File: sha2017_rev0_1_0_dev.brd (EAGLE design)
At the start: 95 x 86 mm, 116 parts, among them IC1 AP7215, IC2 CPT112, IC3 CP210X_USB_UART, IC4 ESP32WROOM32, IC5 MCP73833, IC6 FXL6408, M1 MOTOR10MM, Q1 MMBT2222A, Q2 MMBT2222A, Q3 SI1304 BDL, Q4 MOSFET-PCHANNEL, Q5 MMBT2222A, Q6 MOSFET-PCHANNEL, Q7 MMBT2222A, Q8 MMBT2222A, T1 SI2301DS, X1_ JST-PH3, X701 2908-05WB-MG

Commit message: placed most of the parts
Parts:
- removed GND, SIG, VDD: (no value), wirepad:SMD1,27-2,54
- removed JP1: M05X2SHD_SMD, SparkFun-Connectors:2X5-SHROUDED_SMD
- removed M1: MOTOR10MM, SparkFun-Electromechanical:VIBE-MOTOR-10MM
- added J2: (no value), EAGLE-BOARD-TO-BOARD_CONNECTORS-rev16c:610X12243021
- added R27, R28: 470R, rcl:R0603
- added U$1: MOTOR10MM, badge:VIBE-MOTOR-10MM
- moved C38 207.0 mm to (38.2, 50.1)
- moved R26 205.6 mm to (38.8, 43.8)
- moved IC6 202.0 mm to (38.7, 47.5)
- moved Q8 181.5 mm to (27.5, 54.5)
- moved R11 178.2 mm to (27.5, 52.0), turned to 180 degrees
- moved R25 175.0 mm to (23.2, 52.0)
- moved C37 173.1 mm to (20.7, 53.7), turned to 270 degrees
- moved Q6 172.4 mm to (23.2, 54.6)
- moved R12 172.3 mm to (75.6, 78.6), turned to 180 degrees
- moved Q7 170.7 mm to (71.6, 76.7)
- moved R13 169.4 mm to (70.6, 73.1), turned to 270 degrees
- moved FD2 166.6 mm to (94.6, 86.4)
- moved D14 160.4 mm to (59.9, 74.0)
- moved R16 160.4 mm to (57.1, 74.9)
- moved T1 160.4 mm to (59.9, 76.8)
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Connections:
- removed net N$44: M1.+, R12.1
- removed net WS2812_POWER1: R11.1
- new net N$16: Q7.3, U$1.-
- new net WS2812_DATA_OUT: D9.2, J2.5
- new net WS2812_POWER_EN: IC6.12, R11.1, R18.1
- net +3V3: now also R27.1, R28.1
- net 3V3_SWITCHED: now also J2.12; no longer JP1.1
- net EXTIO-0: now also IC4.9, J2.10; no longer IC4.7, JP1.3
- net EXTIO-1: now also J2.9; no longer JP1.5
- net EXTIO-2: now also J2.8; no longer JP1.7
- net EXTIO-3: now also J2.4; no longer JP1.8
- net EXTIO-4: now also J2.3; no longer JP1.6
- net EXTIO-5: now also J2.2; no longer JP1.4
- net GND: now also J2.1; no longer GND.1, JP1.2, JP1.9
- net I2C_SCL: now also J2.6, R27.2
- net I2C_SDA: now also J2.7, R28.2
- net N$18: now also R12.1, U$1.+; no longer M1.-, Q7.3
- net VBAT: no longer R12.2
- net VBAT_SENSE: now also IC4.7; no longer IC4.9
- net VCC: now also R12.2
- net VUSB_SENSE: now also IC4.6; no longer IC4.8
- net WS2812_DATA: now also IC4.8; no longer IC4.6, SIG.1
- net WS2812_POWER: now also J2.11; no longer IC6.12, JP1.10, R18.1, VDD.1
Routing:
- net LCD_MOSI: track 25.6 -> 13.4 mm
- net LCD_SCK: track 23.6 -> 12.4 mm
- net LCD_CS: track 21.3 -> 11.2 mm
- net VCC: track 13.9 -> 4.67 mm, vias 1 -> 0
- net LCD_D/!S: track 19.0 -> 10.2 mm
- net LCD_!RESET: track 16.8 -> 8.65 mm
- net +3V3: track 11.9 -> 6.54 mm
- net PROXIMITY: track 228.7 -> 224.8 mm
- net +5V: track 34.3 -> 32.9 mm
- net VUSB_SENSE: track 5.10 -> 5.60 mm
- net GND: track 17.5 -> 17.6 mm, vias 63 -> 55
- removed copper zone on layer 16, net VCC
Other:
- board text removed: "MarkusBec"
- board text removed: "RESET"
- board text removed: "SHA Rev0.0.1 Dev"

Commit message: finised routing
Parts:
- removed J2: (no value), EAGLE-BOARD-TO-BOARD_CONNECTORS-rev16c:610X12243021
- added J3: (no value), EAGLE-BOARD-TO-BOARD_CONNECTORS-rev16c:610X12243021
- added S1, S2: SWITCH-MOMENTARY-2SMD, SparkFun-Electromechanical:TACTILE-SWITCH-SMD
- moved R28 76.4 mm to (20.4, 56.5), turned to 90 degrees
- moved R27 73.2 mm to (22.0, 56.5), turned to 90 degrees
- moved R8 29.9 mm to (15.4, 56.5)
- moved C36 22.5 mm to (39.0, 75.3), turned to 180 degrees
- moved R22 20.7 mm to (39.0, 73.8), turned to 0 degrees
- moved R17 16.8 mm to (53.2, 60.7)
- moved R20 16.8 mm to (53.2, 62.4)
- moved C34 16.6 mm to (53.2, 63.9)
- moved R21 15.8 mm to (42.3, 73.8), turned to 0 degrees
- moved C38 11.8 mm to (47.9, 43.3), turned to 270 degrees
- moved IC6 11.7 mm to (50.3, 46.2), turned to 270 degrees
- moved R26 10.6 mm to (49.4, 43.3), turned to 90 degrees
- moved C37 7.81 mm to (22.0, 46.0), turned to 0 degrees
- moved Q8 6.96 mm to (21.0, 52.0), turned to 90 degrees
- moved Q6 6.33 mm to (20.9, 48.7), turned to 270 degrees
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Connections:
- net 3V3_SWITCHED: now also J3.12; no longer J2.12
- net CHRG_STAT: now also IC6.12; no longer IC6.6
- net ESP32_!RESET: now also S2.3
- net ESP32_FLASH/TOUCHE_MENU: now also S1.3
- net EXTIO-0: now also J3.3; no longer J2.10
- net EXTIO-1: now also J3.4; no longer J2.9
- net EXTIO-2: now also J3.5; no longer J2.8
- net EXTIO-3: now also IC6.3, J3.9; no longer IC6.5, J2.4
- net EXTIO-4: now also J3.10; no longer J2.3
- net EXTIO-5: now also IC6.5, J3.11; no longer IC6.3, J2.2
- net GND: now also J3.1, S1.1, S2.1; no longer J2.1
- net I2C_SCL: now also J3.6; no longer J2.6
- net I2C_SDA: now also J3.7; no longer J2.7
- net SD_CD: now also IC6.6; no longer IC6.8
- net WS2812_DATA_OUT: now also J3.8; no longer J2.5
- net WS2812_POWER: now also J3.2; no longer J2.11
- net WS2812_POWER_EN: now also IC6.8; no longer IC6.12
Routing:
- net +3V3: track 6.54 -> 228.0 mm, vias 0 -> 7
- net WS2812_POWER: track 0.00 -> 138.7 mm, vias 0 -> 9
- net WS2812_POWER_EN: track 0.00 -> 116.3 mm, vias 0 -> 7
- net LCD_!RESET: track 8.65 -> 116.4 mm, vias 1 -> 2
- net LCD_BUSY: track 7.67 -> 114.8 mm, vias 1 -> 2
- net LCD_D/!S: track 10.2 -> 111.5 mm, vias 1 -> 2
- net LCD_CS: track 11.2 -> 109.8 mm, vias 1 -> 2
- net LCD_SCK: track 12.4 -> 107.3 mm, vias 1 -> 2
- net LCD_MOSI: track 13.4 -> 106.2 mm, vias 1 -> 2
- net WS2812_DATA_OUT: track 0.00 -> 79.6 mm, vias 0 -> 5
- net VIBRATOR: track 0.00 -> 74.7 mm, vias 0 -> 4
- net I2C_SDA: track 14.0 -> 88.2 mm, vias 0 -> 3
- net I2C_SCL: track 12.6 -> 86.5 mm, vias 0 -> 3
- net ESP32_!RESET: track 0.57 -> 55.1 mm, vias 0 -> 4
- net EXTIO-2: track 0.00 -> 50.5 mm, vias 0 -> 2
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- added copper zone on layer 1, net N$49
- added copper zone on layer 16, net VCC

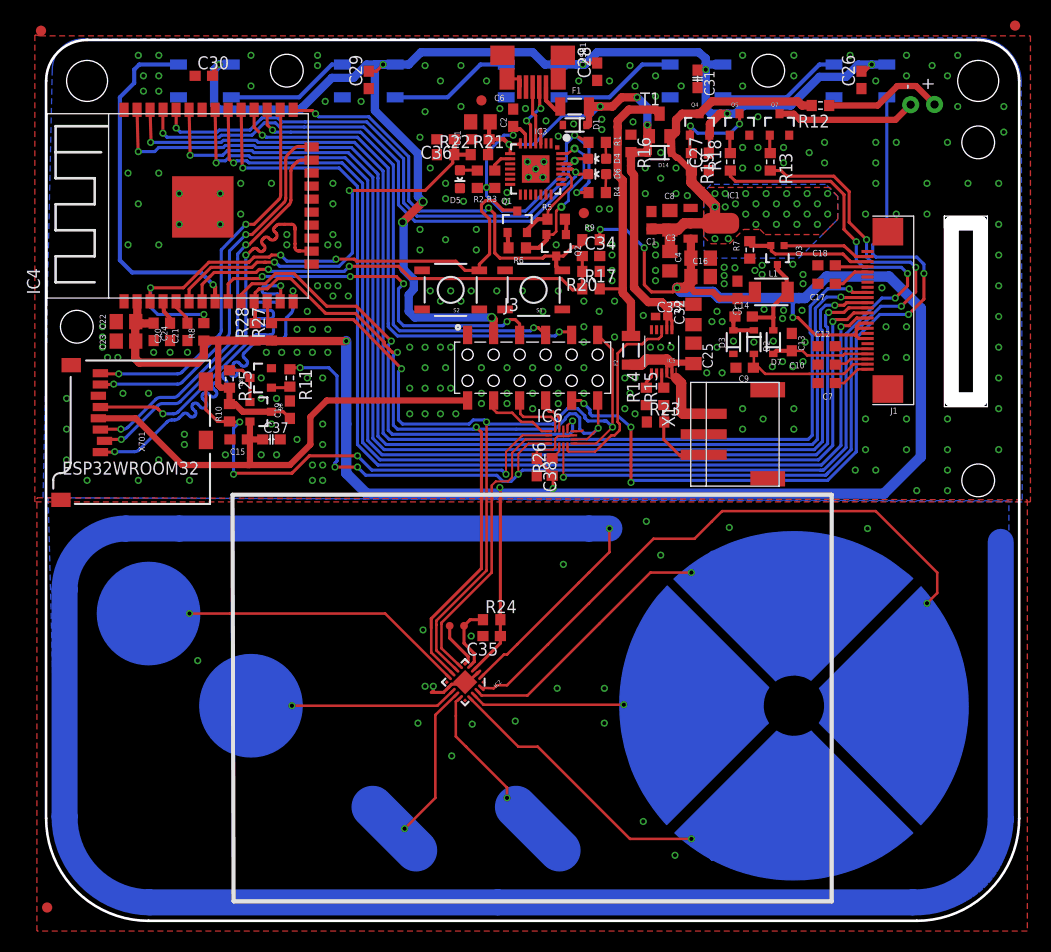
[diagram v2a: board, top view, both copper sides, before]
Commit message: removed some drc errors and add feducials
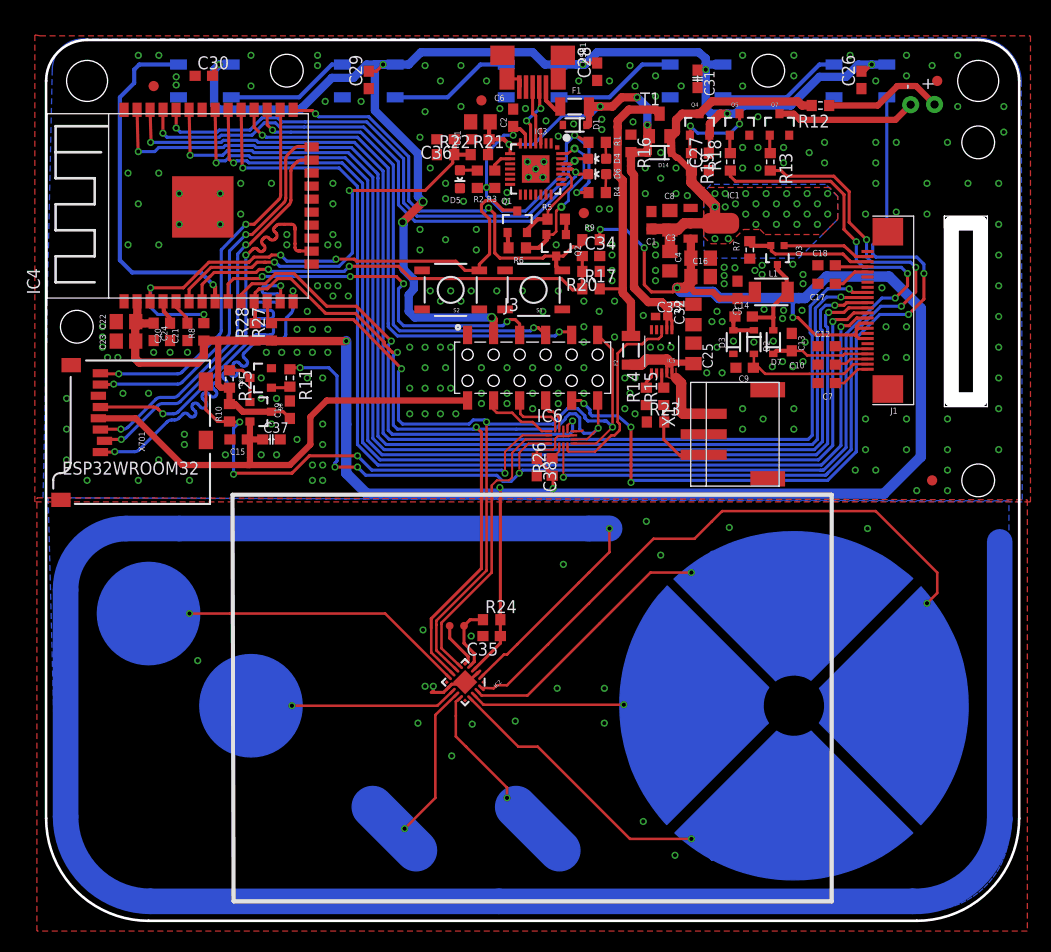
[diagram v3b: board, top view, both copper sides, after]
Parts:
- moved FD5 95.9 mm to (86.5, 42.0)
- moved FD1 12.3 mm to (10.5, 80.5)
- moved FD2 9.32 mm to (87.0, 81.0)
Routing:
- net GND: vias 300 -> 297
